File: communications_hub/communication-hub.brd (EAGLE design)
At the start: 82.5 x 54 mm, 52 parts, among them CON1 SM04B-GHS-TB, CON2 SM04B-GHS-TB, CON3 SM02B-GHS-TB, CON4 SM04B-GHS-TB, CON5 SM04B-GHS-TB, Q1 DMN5L06K, Q2 DMN5L06K, U1 TCAN1042HVDR, U2 TCAN1042HVDR

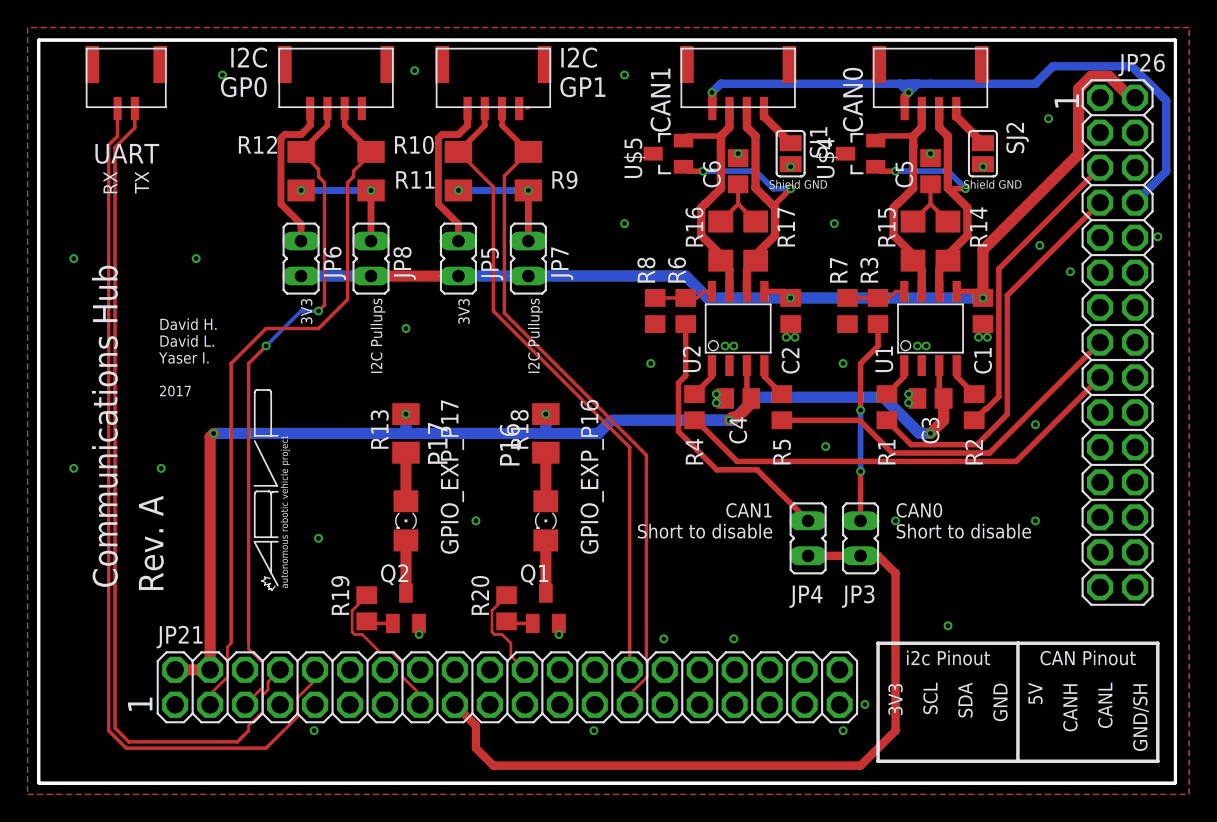
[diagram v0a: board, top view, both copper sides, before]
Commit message: Finally got around to finishing this.
Added test points and power bus indication LEDs.
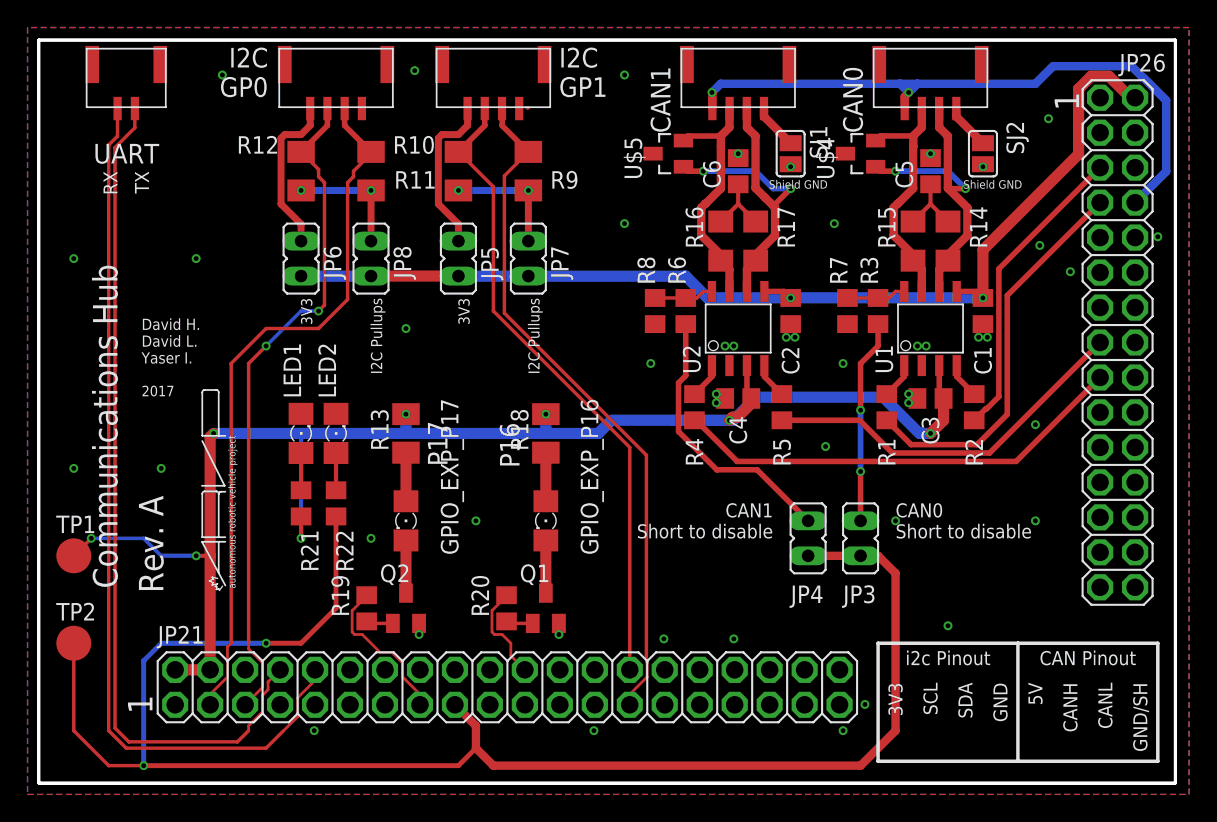
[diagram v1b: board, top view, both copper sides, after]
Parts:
- added LED1, LED2: (no value), led:1206
- added R21: 140, resistor:R0805
- added R22: 66, resistor:R0805
- added TP1, TP2: TPB2,54, testpad:B2,54
- moved U$1 3.81 mm to (14.3, 14.1)
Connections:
- new net N$13: LED1.A, R21.1
- new net N$14: LED2.A, R22.1
- net +3V3: now also R22.2, TP2.TP
- net +5V: now also R21.2, TP1.TP
- net GND: now also LED1.C, LED2.C
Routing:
- net +3V3: track 131.7 -> 198.7 mm, vias 2 -> 4
- net +5V: track 138.8 -> 158.9 mm, vias 7 -> 10
- net N$14: track 0.00 -> 2.71 mm
- net N$13: track 0.00 -> 2.71 mm

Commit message: Added a reference ground test point.
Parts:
- added TP3: TPB2,54, testpad:B2,54
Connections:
- net GND: now also TP3.TP
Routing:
- net +3V3: track 198.7 -> 198.1 mm
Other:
- board text added: "+3v3"
- board text added: "+5v"
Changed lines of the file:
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@@
 <drawing>
 <settings>
-<setting alwaysvectorfont="no"/>
+<setting alwaysvectorfont="yes"/>
 <setting verticaltext="up"/>
 </settings>
-<grid distance="50" unitdist="mil" unit="mil" style="dots" multiple="1" display="yes" altdistance="12.5" altunitdist="mil" altunit="mil"/>
+<grid distance="5" unitdist="mil" unit="mil" style="dots" multiple="1" display="yes" altdistance="12.5" altunitdist="mil" altunit="mil"/>
 <layers>
 <layer number="1" name="Top" color="4" fill="1" visible="yes" active="yes"/>
@@
 <wire x1="71.12" y1="10.16" x2="60.96" y2="10.16" width="0.254" layer="21"/>
 <wire x1="71.12" y1="1.5875" x2="71.12" y2="10.16" width="0.254" layer="21"/>
+<text x="0.127" y="0.254" size="1.778" layer="21">GND</text>
+<text x="6.096" y="6.731" size="1.778" layer="21" rot="R90">+3v3</text>
+<text x="3.302" y="18.034" size="1.778" layer="21" rot="R90">+5v</text>
 </plain>
 <attributes>
@@
 <attribute name="VALUE" x="19.05" y="20.955" size="1.27" layer="27" rot="R270"/>
 </element>
-<element name="TP1" library="testpad" library_urn="urn:adsk.eagle:library:385" package="B2,54" package3d_urn="urn:adsk.eagle:package:27948/1" value="TPB2,54" x="2.54" y="16.51">
-<attribute name="TP_SIGNAL_NAME" value="" x="2.54" y="16.51" size="1.778" layer="27" display="off"/>
-</element>
-<element name="TP2" library="testpad" library_urn="urn:adsk.eagle:library:385" package="B2,54" package3d_urn="urn:adsk.eagle:package:27948/1" value="TPB2,54" x="2.54" y="10.16">
-<attribute name="TP_SIGNAL_NAME" value="" x="2.54" y="10.16" size="1.778" layer="27" display="off"/>
+<element name="TP1" library="testpad" library_urn="urn:adsk.eagle:library:385" package="B2,54" package3d_urn="urn:adsk.eagle:package:27948/1" value="TPB2,54" x="2.54" y="16.51" smashed="yes">
+<attribute name="NAME" x="1.27" y="18.161" size="1.27" layer="25" ratio="10" display="off"/>
+<attribute name="TP_SIGNAL_NAME" value="" x="1.27" y="13.335" size="1" layer="37"/>
+<attribute name="VALUE" x="1.27" y="15.113" size="0.0254" layer="27"/>
+</element>
+<element name="TP2" library="testpad" library_urn="urn:adsk.eagle:library:385" package="B2,54" package3d_urn="urn:adsk.eagle:package:27948/1" value="TPB2,54" x="2.54" y="10.16" smashed="yes">
+<attribute name="NAME" x="1.27" y="11.811" size="1.27" layer="25" ratio="10" display="off"/>
+<attribute name="TP_SIGNAL_NAME" value="" x="1.27" y="6.985" size="1" layer="37"/>
+<attribute name="VALUE" x="1.27" y="8.763" size="0.0254" layer="27"/>
+</element>
+<element name="TP3" library="testpad" library_urn="urn:adsk.eagle:library:385" package="B2,54" package3d_urn="urn:adsk.eagle:package:27948/1" value="TPB2,54" x="2.54" y="3.81" smashed="yes">
+<attribute name="NAME" x="1.27" y="5.461" size="1.27" layer="25" ratio="10" display="off"/>
+<attribute name="TP_SIGNAL_NAME" value="" x="1.27" y="0.635" size="1" layer="37"/>
+<attribute name="VALUE" x="1.27" y="2.413" size="0.0254" layer="27"/>
 </element>
 </elements>
@@
 <contactref element="LED1" pad="C"/>
 <contactref element="LED2" pad="C"/>
+<contactref element="TP3" pad="TP"/>
 </signal>
 <signal name="+3V3">
@@
 <wire x1="7.62" y1="8.89" x2="8.89" y2="10.16" width="0.3556" layer="16"/>
 <contactref element="TP2" pad="TP"/>
-<wire x1="7.62" y1="1.27" x2="5.08" y2="1.27" width="0.254" layer="1"/>
-<wire x1="5.08" y1="1.27" x2="2.54" y2="3.81" width="0.254" layer="1"/>
-<wire x1="2.54" y1="3.81" x2="2.54" y2="10.16" width="0.254" layer="1"/>
+<wire x1="7.62" y1="1.27" x2="6.35" y2="1.27" width="0.254" layer="1"/>
+<wire x1="6.35" y1="1.27" x2="4.445" y2="3.175" width="0.254" layer="1"/>
+<wire x1="4.445" y1="4.699" x2="2.413" y2="6.731" width="0.254" layer="1"/>
+<wire x1="2.413" y1="6.731" x2="2.413" y2="10.033" width="0.254" layer="1"/>
+<wire x1="2.413" y1="10.033" x2="2.54" y2="10.16" width="0.254" layer="1"/>
+<wire x1="4.445" y1="3.175" x2="4.445" y2="4.699" width="0.254" layer="1"/>
 <wire x1="21.59" y1="19.37" x2="24.13" y2="36.83" width="0" layer="19" extent="1-1"/>
 <wire x1="9.906" y1="5.6896" x2="7.62" y2="8.89" width="0" layer="19" extent="16-16"/>

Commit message: Fixed issues.
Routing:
- net +3V3: track 198.1 -> 200.4 mm
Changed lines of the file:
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@@
 <drawing>
 <settings>
-<setting alwaysvectorfont="yes"/>
+<setting alwaysvectorfont="no"/>
 <setting verticaltext="up"/>
 </settings>
@@
 <wire x1="30.48" y1="1.27" x2="7.62" y2="1.27" width="0.3556" layer="1"/>
 <via x="7.62" y="1.27" extent="1-16" drill="0.35"/>
-<wire x1="7.62" y1="1.27" x2="7.62" y2="8.89" width="0.3556" layer="16"/>
+<wire x1="7.62" y1="1.27" x2="7.62" y2="5.715" width="0.3556" layer="16"/>
 <via x="16.51" y="10.16" extent="1-16" drill="0.35"/>
+<wire x1="7.62" y1="5.715" x2="7.62" y2="8.89" width="0.3556" layer="16"/>
 <wire x1="8.89" y1="10.16" x2="16.51" y2="10.16" width="0.3556" layer="16"/>
 <wire x1="16.51" y1="10.16" x2="19.05" y2="10.16" width="0.3556" layer="1"/>
@@
 <wire x1="2.413" y1="10.033" x2="2.54" y2="10.16" width="0.254" layer="1"/>
 <wire x1="4.445" y1="3.175" x2="4.445" y2="4.699" width="0.254" layer="1"/>
+<wire x1="9.906" y1="5.6896" x2="7.6454" y2="5.6896" width="0.3048" layer="16"/>
+<wire x1="7.6454" y1="5.6896" x2="7.62" y2="5.715" width="0.3048" layer="16"/>
 <wire x1="21.59" y1="19.37" x2="24.13" y2="36.83" width="0" layer="19" extent="1-1"/>
-<wire x1="9.906" y1="5.6896" x2="7.62" y2="8.89" width="0" layer="19" extent="16-16"/>
 </signal>
 <signal name="CAN0_RX_T">

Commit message: Generated updated CAM files.
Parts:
- removed U$3: (no value), frames:DOCFIELD
- U$2: device frames:LETTER_P -> frames:A4L-LOC
- moved U$2 55.2 mm to (-86.0, -70.7)
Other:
- board text added: "2"
- board text added: "2018"
- board text added: "Rev. 2.0"
- board text added: "Revision"
- board text removed: "2017"
- board text removed: "Rev. A"

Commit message: Fixed a typo
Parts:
- R12: value 100K -> 10K
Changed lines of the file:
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@@
 <attribute name="VALUE" x="21.59" y="45.72" size="1.27" layer="27" rot="R270"/>
 </element>
-<element name="R12" library="resistor" library_urn="urn:adsk.eagle:library:348" package="M1206" package3d_urn="urn:adsk.eagle:package:23566/1" value="100K" x="19.05" y="44.45" smashed="yes" rot="R270">
+<element name="R12" library="resistor" library_urn="urn:adsk.eagle:library:348" package="M1206" package3d_urn="urn:adsk.eagle:package:23566/1" value="10K" x="19.05" y="44.45" smashed="yes" rot="R270">
 <attribute name="NAME" x="17.3355" y="45.212" size="1.27" layer="25" rot="R180" align="top-left"/>
 <attribute name="VALUE" x="16.51" y="45.72" size="1.27" layer="27" rot="R270"/>
